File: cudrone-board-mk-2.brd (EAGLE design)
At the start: 100 x 70 mm, 3 parts, among them U1 EDISON_CONNECTOR_FULLMOUNTING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

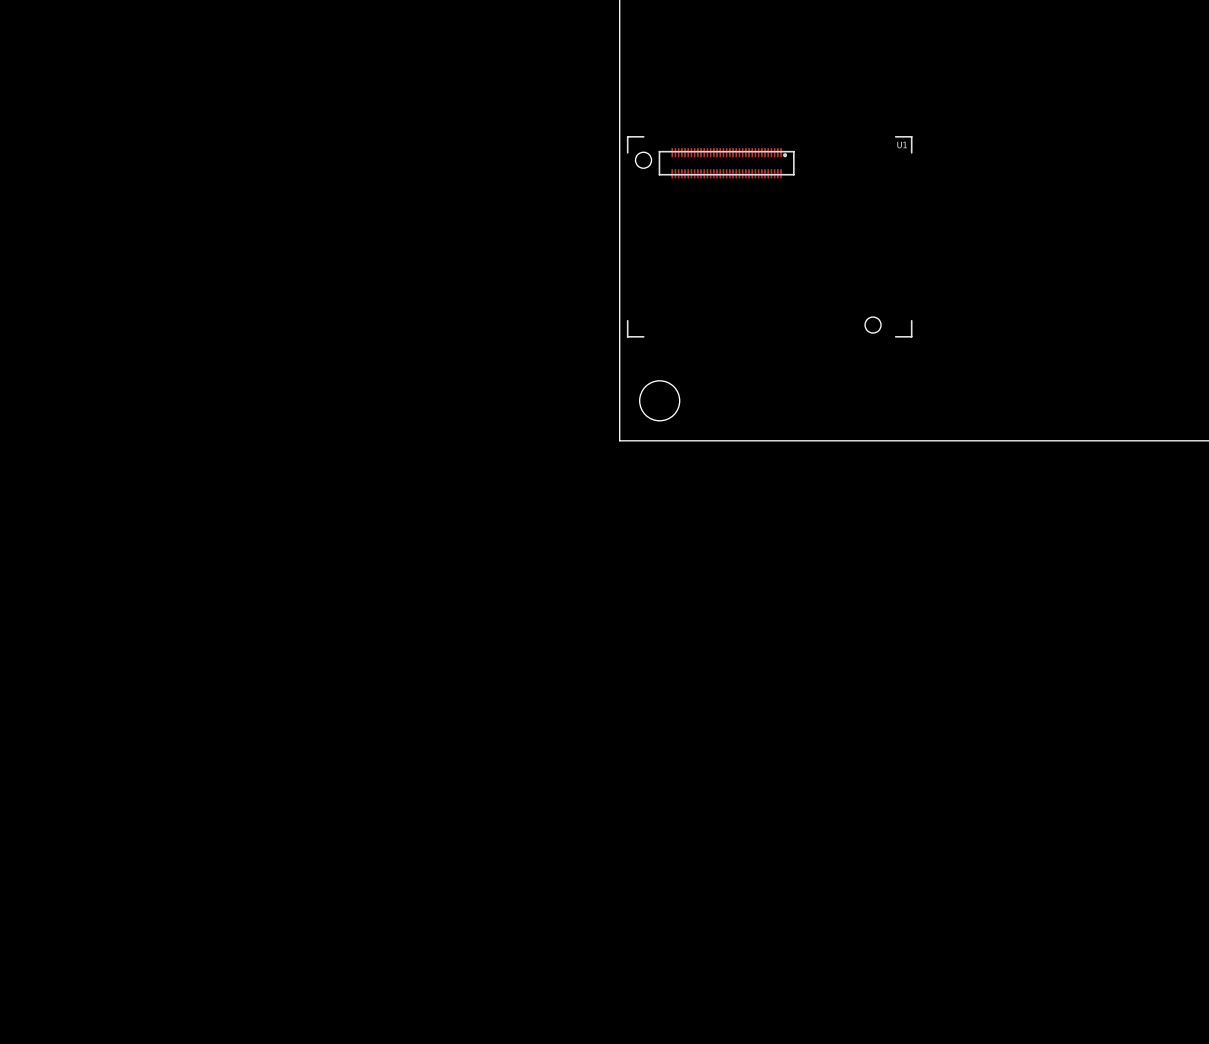
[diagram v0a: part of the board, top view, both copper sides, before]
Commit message: Labeled edison nets and added RTC backup battery
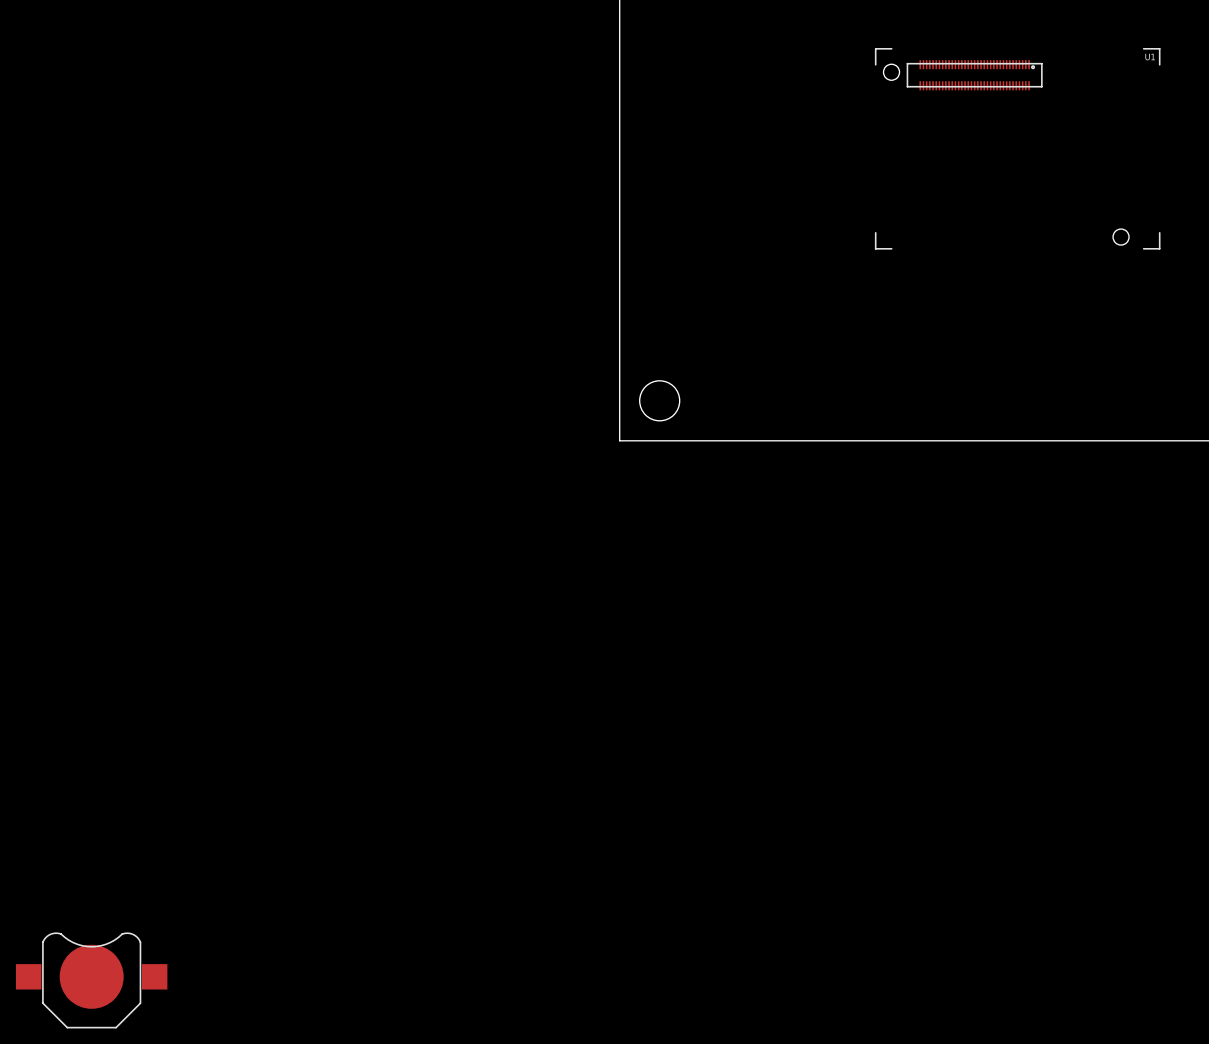
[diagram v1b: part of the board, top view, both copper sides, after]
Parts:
- added BAT_BACKUP: RTC backup battery, SparkFun-Electromechanical:BATTCON_12MM
- moved U1 32.9 mm to (32.0, 49.0)
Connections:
- new net 1.8V: U1.12
- new net 3.3V: U1.10, U1.8
- new net DCIN: U1.14
- new net FAULT: U1.19
- new net FW_RCVR: U1.69
- new net GND: BAT_BACKUP.GND, U1.1, U1.11, U1.13, U1.15, U1.5, U1.9
- new net GP109_SPI_2_CLK: U1.55
- new net GP110_SPI_2_FS0: U1.53
- new net GP111_SPI_2_FS1: U1.51
- new net GP114_SPI_2_RXD: U1.59
- new net GP115_SPI_2_TXD: U1.57
- new net GP128_UART_1_CTS: U1.65
- new net GP129_UART_1_RTS: U1.63
- new net GP12_PWM0: U1.35
- new net GP130_UART_1_RX: U1.61
- new net GP131_UART_1_TX: U1.46
- new net GP134_UART_2_RX: U1.22
- new net GP135_UART_2_TX: U1.27
- new net GP13_PWM1: U1.33
- new net GP14: U1.48
- new net GP15: U1.42
- new net GP165: U1.25
- new net GP182_PWM2: U1.37
- new net GP183_PWM3: U1.39
- new net GP19_I2C_1_SCL: U1.41
- new net GP20_I2C_1_SDA: U1.43
- new net GP27_I2C_6_SCL: U1.45
- new net GP28_I2C_6_SDA: U1.47
- new net GP40_I2S_2_CLK: U1.52
- new net GP41_I2S_2_FS: U1.54
- new net GP42_I2S_2_RXD: U1.50
- new net GP43_I2S_2_TXD: U1.56
- new net GP44: U1.24
- new net GP45: U1.26
- new net GP46: U1.28
- new net GP47: U1.30
- new net GP48: U1.32
- new net GP49: U1.34
- new net GP77_SD_0_CD#: U1.60
- new net GP78_SD_0_CLK: U1.58
- new net GP79_SD_0_CMD: U1.62
- new net GP80_SD_0_DAT0: U1.66
- new net GP81_SD_0_DAT1: U1.70
- new net GP82_SD_0_DAT2: U1.64
- new net GP83_SD_0_DAT3: U1.68
- new net GP84_SD_CLK_FB: U1.44
- new net MSIC_SLP_CLK: U1.7
- new net OSC_CLK_OUT: U1.67
- new net PSW: U1.21
- new net PWRBTN#: U1.17
- new net RCVR_MODE: U1.31
- new net RESET_OUT#: U1.36
- new net USB_DN: U1.18
- new net USB_DP: U1.16
- new net USB_ID: U1.3
- new net USB_VBUS: U1.20
- new net VSYS: U1.2, U1.4, U1.6
- new net V_BAT_BKUP: BAT_BACKUP.PWR@1, U1.23
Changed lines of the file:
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@@
 <element name="U$1" library="frames" package="LETTER_L" value="" x="-75.5" y="-59"/>
 <element name="U$2" library="frames" package="DOCFIELD" value="" x="71.5" y="-59"/>
-<element name="U1" library="SparkFun-Boards" package="EDISON_DAUGHTER" value="EDISON_CONNECTOR_FULLMOUNTING_HOLES" x="1" y="38" rot="R270"/>
+<element name="U1" library="SparkFun-Boards" package="EDISON_DAUGHTER" value="EDISON_CONNECTOR_FULLMOUNTING_HOLES" x="32" y="49" rot="R270"/>
+<element name="BAT_BACKUP" library="SparkFun-Electromechanical" package="BATTCON_12MM" value="RTC backup battery" x="-66" y="-67">
+<attribute name="PROD_ID" value="BATT-08044" x="-66" y="-67" size="1.778" layer="27" display="off"/>
+</element>
 </elements>
 <signals>
+<signal name="GND">
+<contactref element="BAT_BACKUP" pad="GND"/>
+<contactref element="U1" pad="1"/>
+<contactref element="U1" pad="5"/>
+<contactref element="U1" pad="9"/>
+<contactref element="U1" pad="11"/>
+<contactref element="U1" pad="13"/>
+<contactref element="U1" pad="15"/>
+<wire x1="48.37" y1="47.02" x2="-66" y2="-67" width="0" layer="19" extent="1-1"/>
+<wire x1="48.77" y1="47.02" x2="48.37" y2="47.02" width="0" layer="19" extent="1-1"/>
+<wire x1="49.17" y1="47.02" x2="48.77" y2="47.02" width="0" layer="19" extent="1-1"/>
+<wire x1="49.57" y1="47.02" x2="49.17" y2="47.02" width="0" layer="19" extent="1-1"/>
+<wire x1="50.37" y1="47.02" x2="49.57" y2="47.02" width="0" layer="19" extent="1-1"/>
+<wire x1="51.17" y1="47.02" x2="50.37" y2="47.02" width="0" layer="19" extent="1-1"/>
+</signal>
+<signal name="V_BAT_BKUP">
+<contactref element="BAT_BACKUP" pad="PWR@1"/>
+<contactref element="U1" pad="23"/>
+<wire x1="46.77" y1="47.02" x2="-73.874" y2="-67" width="0" layer="19" extent="1-1"/>
+</signal>
+<signal name="VSYS">
+<contactref element="U1" pad="2"/>
+<contactref element="U1" pad="4"/>
+<contactref element="U1" pad="6"/>
+<wire x1="50.77" y1="44.38" x2="51.17" y2="44.38" width="0" layer="19" extent="1-1"/>
+<wire x1="50.37" y1="44.38" x2="50.77" y2="44.38" width="0" layer="19" extent="1-1"/>
+</signal>
+<signal name="3.3V">
+<contactref element="U1" pad="8"/>
+<contactref element="U1" pad="10"/>
+<wire x1="49.57" y1="44.38" x2="49.97" y2="44.38" width="0" layer="19" extent="1-1"/>
+</signal>
+<signal name="GP183_PWM3">
+<contactref element="U1" pad="39"/>
+</signal>
+<signal name="GP182_PWM2">
+<contactref element="U1" pad="37"/>
+</signal>
+<signal name="GP13_PWM1">
+<contactref element="U1" pad="33"/>
+</signal>
+<signal name="GP12_PWM0">
+<contactref element="U1" pad="35"/>
+</signal>
+<signal name="GP14">
+<contactref element="U1" pad="48"/>
+</signal>
+<signal name="GP15">
+<contactref element="U1" pad="42"/>
+</signal>
+<signal name="GP49">
+<contactref element="U1" pad="34"/>
+</signal>
+<signal name="GP48">
+<contactref element="U1" pad="32"/>
+</signal>
+<signal name="GP47">
+<contactref element="U1" pad="30"/>
+</signal>
+<signal name="GP46">
+<contactref element="U1" pad="28"/>
+</signal>
+<signal name="GP45">
+<contactref element="U1" pad="26"/>
+</signal>
+<signal name="GP165">
+<contactref element="U1" pad="25"/>
+</signal>
+<signal name="GP44">
+<contactref element="U1" pad="24"/>
+</signal>
+<signal name="PSW">
+<contactref element="U1" pad="21"/>
+</signal>
+<signal name="FAULT">
+<contactref element="U1" pad="19"/>
+</signal>
+<signal name="USB_VBUS">
+<contactref element="U1" pad="20"/>
+</signal>
+<signal name="USB_DN">
+<contactref element="U1" pad="18"/>
+</signal>
+<signal name="USB_DP">
+<contactref element="U1" pad="16"/>
+</signal>
+<signal name="USB_ID">
+<contactref element="U1" pad="3"/>
+</signal>
+<signal name="MSIC_SLP_CLK">
+<contactref element="U1" pad="7"/>
+</signal>
+<signal name="RESET_OUT#">
+<contactref element="U1" pad="36"/>
+</signal>
+<signal name="PWRBTN#">
+<contactref element="U1" pad="17"/>
+</signal>
+<signal name="1.8V">
+<contactref element="U1" pad="12"/>
+</signal>
+<signal name="DCIN">
+<contactref element="U1" pad="14"/>
+</signal>
+<signal name="GP114_SPI_2_RXD">
+<contactref element="U1" pad="59"/>
+</signal>
+<signal name="GP115_SPI_2_TXD">
+<contactref element="U1" pad="57"/>
+</signal>
+<signal name="GP109_SPI_2_CLK">
+<contactref element="U1" pad="55"/>
+</signal>
+<signal name="GP110_SPI_2_FS0">
+<contactref element="U1" pad="53"/>
+</signal>
+<signal name="GP111_SPI_2_FS1">
+<contactref element="U1" pad="51"/>
+</signal>
+<signal name="GP135_UART_2_TX">
+<contactref element="U1" pad="27"/>
+</signal>
+<signal name="GP134_UART_2_RX">
+<contactref element="U1" pad="22"/>
+</signal>
+<signal name="GP43_I2S_2_TXD">
+<contactref element="U1" pad="56"/>
+</signal>
+<signal name="GP41_I2S_2_FS">
+<contactref element="U1" pad="54"/>
+</signal>
+<signal name="GP40_I2S_2_CLK">
+<contactref element="U1" pad="52"/>
+</signal>
+<signal name="GP42_I2S_2_RXD">
+<contactref element="U1" pad="50"/>
+</signal>
+<signal name="GP28_I2C_6_SDA">
+<contactref element="U1" pad="47"/>
+</signal>
+<signal name="GP27_I2C_6_SCL">
+<contactref element="U1" pad="45"/>
+</signal>
+<signal name="GP20_I2C_1_SDA">
+<contactref element="U1" pad="43"/>
+</signal>
+<signal name="GP19_I2C_1_SCL">
+<contactref element="U1" pad="41"/>
+</signal>
+<signal name="GP131_UART_1_TX">
+<contactref element="U1" pad="46"/>
+</signal>
+<signal name="GP130_UART_1_RX">
+<contactref element="U1" pad="61"/>
+</signal>
+<signal name="GP129_UART_1_RTS">
+<contactref element="U1" pad="63"/>
+</signal>
+<signal name="GP128_UART_1_CTS">
+<contactref element="U1" pad="65"/>
+</signal>
+<signal name="GP84_SD_CLK_FB">
+<contactref element="U1" pad="44"/>
+</signal>
+<signal name="GP78_SD_0_CLK">
+<contactref element="U1" pad="58"/>
+</signal>
+<signal name="GP77_SD_0_CD#">
+<contactref element="U1" pad="60"/>
+</signal>
+<signal name="GP79_SD_0_CMD">
+<contactref element="U1" pad="62"/>
+</signal>
+<signal name="GP80_SD_0_DAT0">
+<contactref element="U1" pad="66"/>
+</signal>
+<signal name="GP81_SD_0_DAT1">
+<contactref element="U1" pad="70"/>
+</signal>
+<signal name="GP82_SD_0_DAT2">
+<contactref element="U1" pad="64"/>
+</signal>
+<signal name="GP83_SD_0_DAT3">
+<contactref element="U1" pad="68"/>
+</signal>
+<signal name="FW_RCVR">
+<contactref element="U1" pad="69"/>
+</signal>
+<signal name="RCVR_MODE">
+<contactref element="U1" pad="31"/>
+</signal>
+<signal name="OSC_CLK_OUT">
+<contactref element="U1" pad="67"/>
+</signal>
 </signals>
 </board>

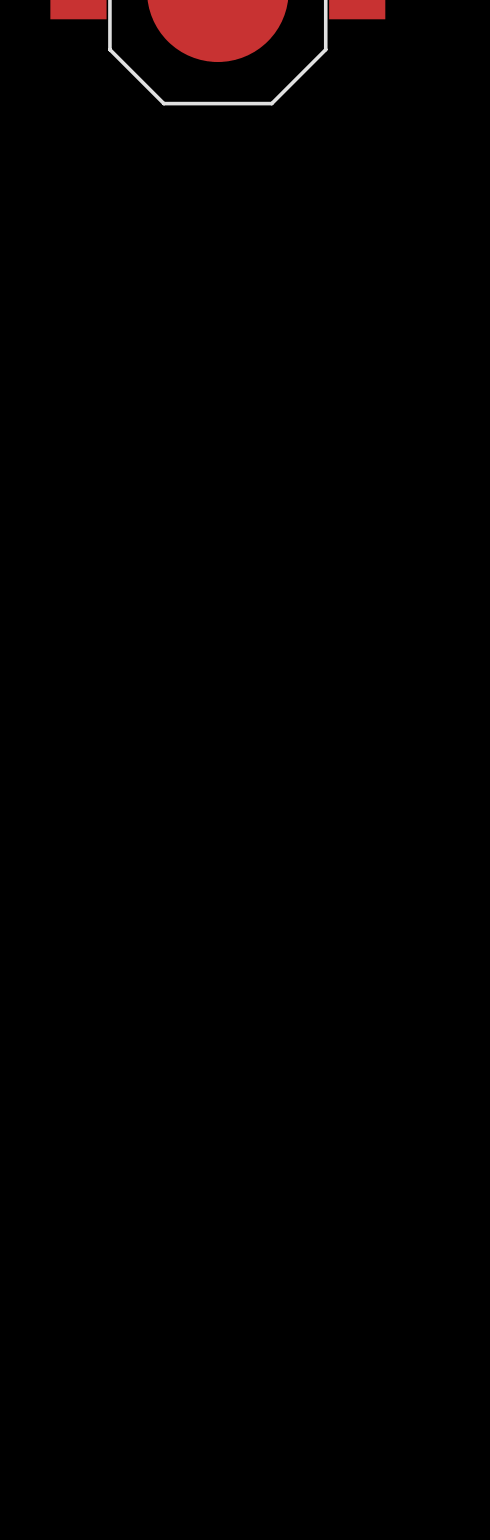
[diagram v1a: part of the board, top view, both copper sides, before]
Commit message: Added contents of base block to schematic
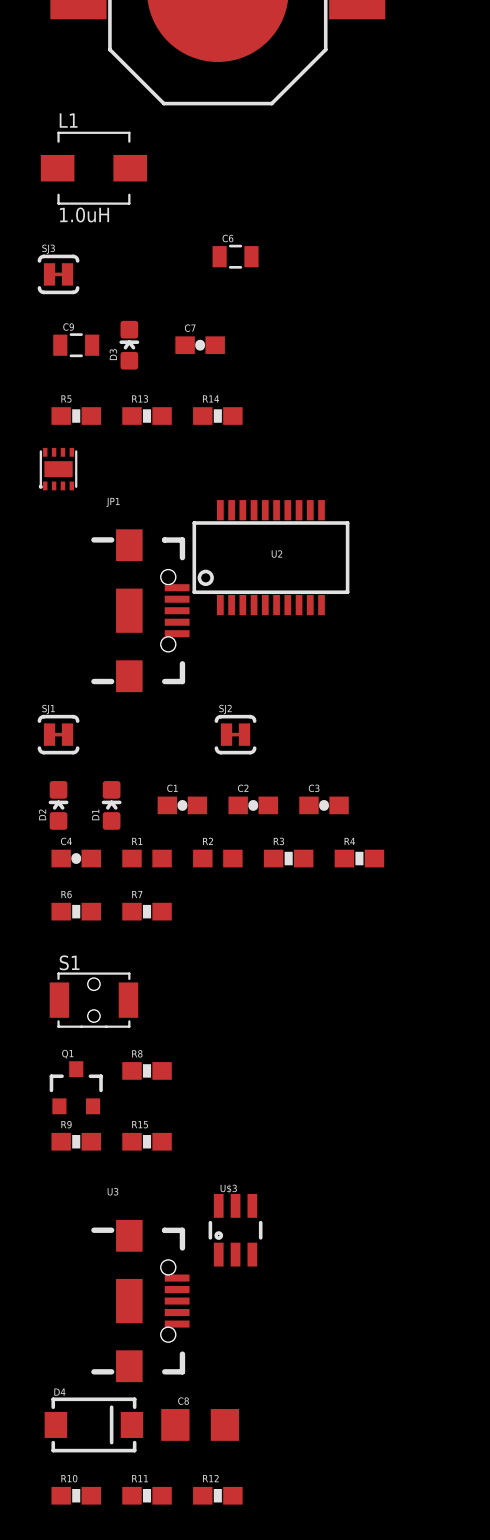
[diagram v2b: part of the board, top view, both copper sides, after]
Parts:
- added C1, C2: 0.1uF, SparkFun-Capacitors:0603-CAP
- added C3, C4, C7: 47pF, SparkFun-Capacitors:0603-CAP
- added C6, C9: 22uF, SparkFun-Capacitors:0805
- added C8: 10uF, SparkFun-Capacitors:1206
- added D1: RED, SparkFun-LED:LED-0603
- added D2: YELLOW, SparkFun-LED:LED-0603
- added D3: BLUE, SparkFun-LED:LED-0603
- added D4: (no value), SparkFun-DiscreteSemi:SMA-DIODE
- added JP1: USB_MICROB, SparkFun-Connectors:USB-B-MICRO-SMD_V03
- added L1: 1.0uH, SparkFun-Passives:INDUCTOR-SRP4020
- added Q1: BSS138, SparkFun-DiscreteSemi:SOT23-3
- added R1, R2: 27, SparkFun-Resistors:0603
- added R10: 287, SparkFun-Resistors:0603-RES
- added R11, R8: 10K, SparkFun-Resistors:0603-RES
- added R12: 100k, SparkFun-Resistors:0603-RES
- added R13: 680k, SparkFun-Resistors:0603-RES
- added R14: 120k, SparkFun-Resistors:0603-RES
- added R15, R3, R4, R5: 1K, SparkFun-Resistors:0603-RES
- added R6, R7: 100, SparkFun-Resistors:0603-RES
- added R9: 220, SparkFun-Resistors:0603-RES
- added S1: POWER, SparkFun-Electromechanical:TACTILE_SWITCH-SMD-RIGHT-ANGLE
- added SJ1, SJ2, SJ3: JUMPER-PAD-2-NC_BY_TRACE, SparkFun-Passives:PAD-JUMPER-2-NC_BY_TRACE_YES_SILK
- added U$3: MIC2039, Testing:SOT23-6
- added U2: FTS31XS-U, SparkFun-DigitalIC:SSOP20_L
- added U3: (no value), SparkFun-Connectors:USB-AB-MICRO-SMD_V03
- added U4: TPS62065, Testing:WSON-8-PAD
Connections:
- new net 5V: C2.2, C9.1, D4.C, JP1.VBUS1, R15.2, U$3.1, U2.15, U4.5, U4.7, U4.8
- new net N$1: SJ1.1, U2.17
- new net N$10: D2.C, R4.2
- new net N$11: R6.1, U2.20
- new net N$12: D3.C, R5.2
- new net N$13: R5.1, SJ3.2
- new net N$14: R7.1, U2.4
- new net N$15: R8.2, R9.2, S1.1
- new net N$16: R10.2, U$3.5
- new net N$17: C7.2, R13.1, R14.2, U4.4
- new net N$18: Q1.1, R15.1
- new net N$19: L1.P$1, U4.2
- new net N$2: C3.1, JP1.D-1, R1.1
- new net N$3: C4.1, JP1.D+1, R2.1
- new net N$4: R1.2, U2.12
- new net N$5: R2.2, U2.11
- new net N$6: SJ2.1, U2.10
- new net N$7: R3.1, SJ1.2
- new net N$8: R4.1, SJ2.2
- new net N$9: D1.C, R3.2
- net 1.8V: now also C1.2, R11.1, U2.14, U2.3
- net DCIN: now also Q1.2
- net FAULT: now also R11.2, U$3.4
- net GND: now also C1.1, C2.1, C3.2, C4.2, C6.2, C8.2, C9.2, JP1.GND1, JP1.SHIELD1, JP1.SHIELD2, JP1.SHIELD3, R10.1, R12.1, R14.1, S1.2, SJ3.1, U$3.2, U2.16, U2.6, U3.GND1, U4.1, U4.3, U4.6, U4.PAD
- net GP134_UART_2_RX: now also R6.2
- net GP135_UART_2_TX: now also R7.2
- net PSW: now also R12.2, U$3.3
- net PWRBTN#: now also R9.1
- net USB_DN: now also U3.D-1
- net USB_DP: now also U3.D+1
- net USB_ID: now also U3.ID1
- net USB_VBUS: now also C8.1, D4.A, U$3.6, U3.VBUS1
- net VSYS: now also C6.1, C7.1, D1.A, D2.A, D3.A, L1.P$2, Q1.3, R13.2, R8.1
